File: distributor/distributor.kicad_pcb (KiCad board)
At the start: 2 copper layers, 91.5 x 52 mm, 38 parts, among them J1 Cerebellum, J10 CAN FD, J11 CAN FD, J12 CAN FD, J13 CAN FD, J14 ArmR, J15 CAN FD, J16 ArmL, J2 Cerebrum, J3 PowerBack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

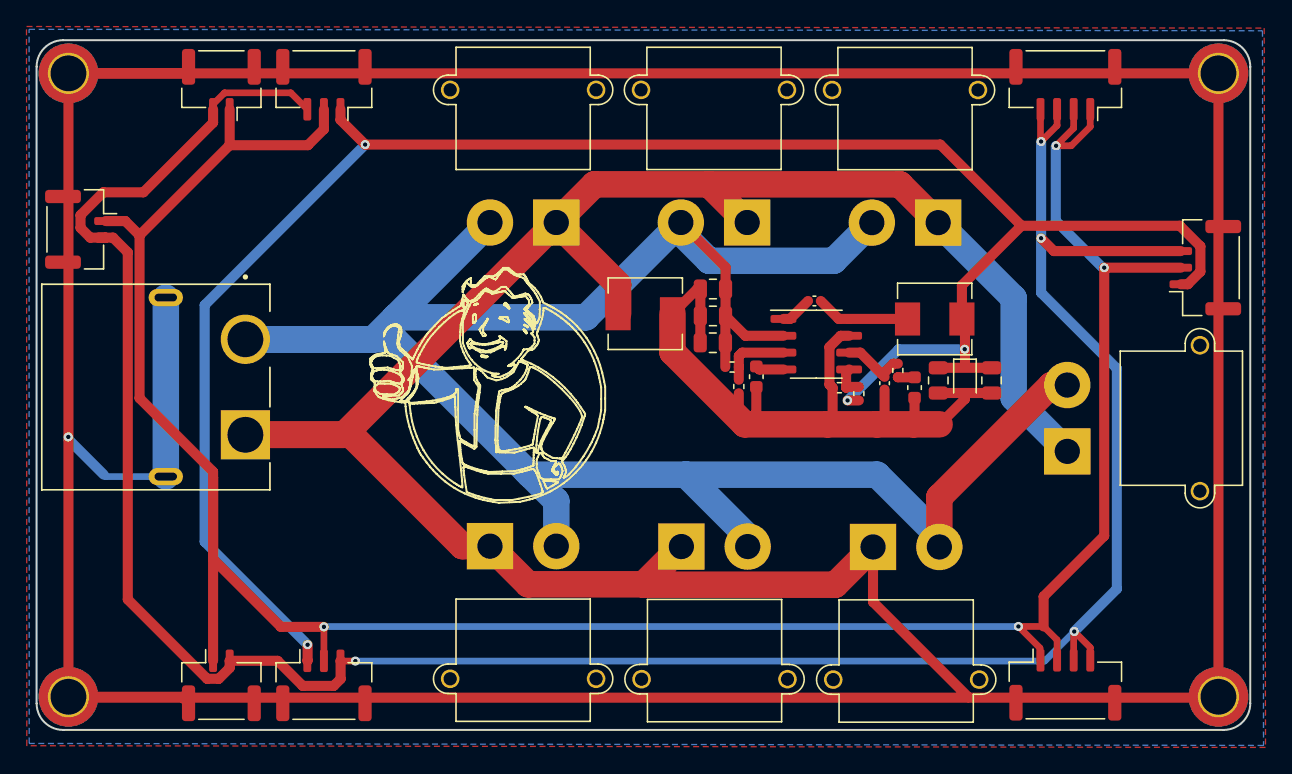
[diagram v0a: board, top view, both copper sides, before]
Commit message: [Fix] Manufacture modification
Signed-off-by: Homalozoa <nx.tardis@gmail.com>
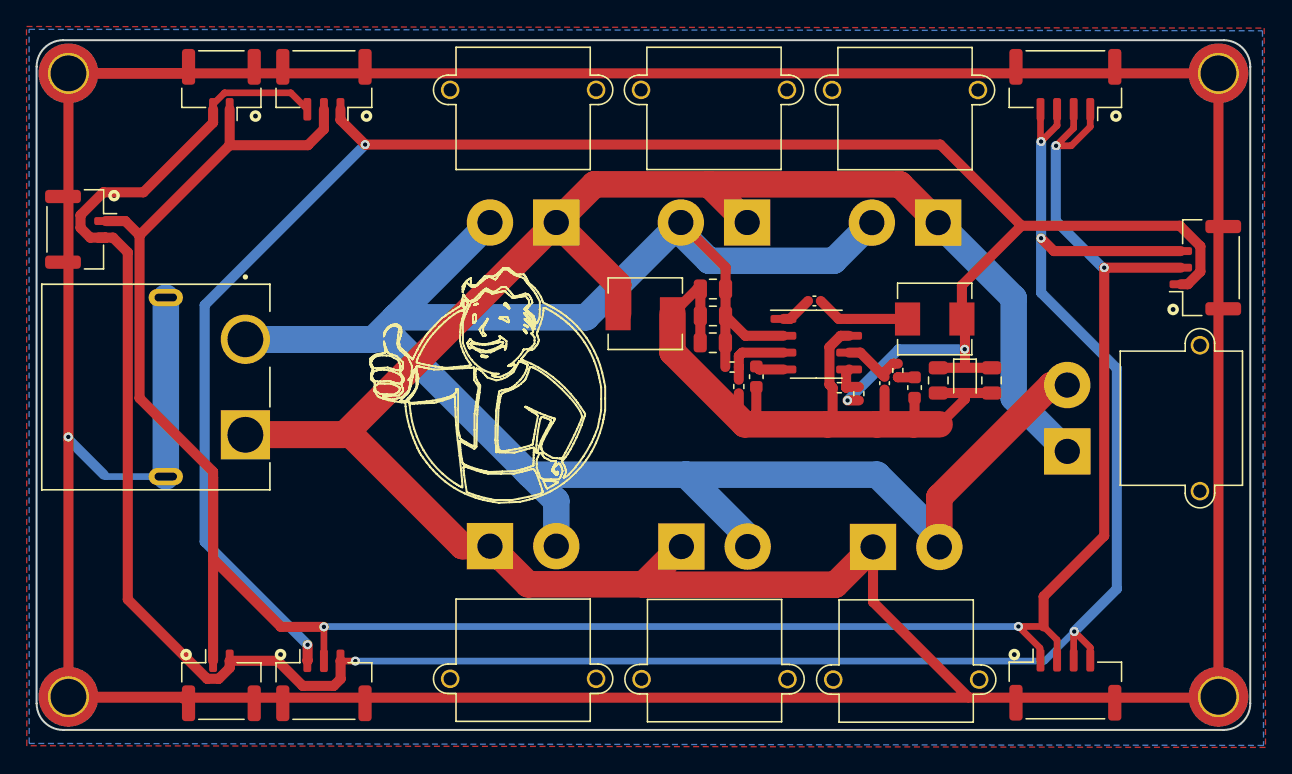
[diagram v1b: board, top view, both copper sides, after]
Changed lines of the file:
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@@
   (gr_arc (start 137.393529 98.762622) (mid 137.397287 98.760088) (end 137.401781 98.75955) (layer "F.SilkS") (width 0.15))
   (gr_line (start 143.124717 106.484575) (end 143.280318 106.639646) (layer "F.SilkS") (width 0.15))
+  (gr_circle (center 122.641 120.32) (end 122.95 120.32) (layer "F.SilkS") (width 0.254) (fill none))
   (gr_line (start 142.924024 102.971644) (end 142.689915 103.401539) (layer "F.SilkS") (width 0.15))
   (gr_arc (start 137.317254 94.651959) (mid 137.332678 94.665701) (end 137.345481 94.681916) (layer "F.SilkS") (width 0.15))
@@
   (gr_line (start 142.783427 99.367457) (end 143.299443 99.795497) (layer "F.SilkS") (width 0.15))
   (gr_line (start 131.874717 98.518776) (end 131.874717 98.292853) (layer "F.SilkS") (width 0.15))
+  (gr_circle (center 115.521 120.32) (end 115.83 120.32) (layer "F.SilkS") (width 0.254) (fill none))
   (gr_line (start 129.606263 98.677151) (end 129.57722 98.608727) (layer "F.SilkS") (width 0.15))
   (gr_line (start 138.892062 91.999983) (end 138.933694 91.937269) (layer "F.SilkS") (width 0.15))
@@
   (gr_arc (start 137.260439 95.292505) (mid 137.232883 95.299262) (end 137.204602 95.301539) (layer "F.SilkS") (width 0.15))
   (gr_line (start 146.814717 101.042419) (end 146.814717 101.917343) (layer "F.SilkS") (width 0.15))
+  (gr_circle (center 120.75 79.72) (end 121.059 79.72) (layer "F.SilkS") (width 0.254) (fill none))
   (gr_line (start 139.292217 92.954137) (end 139.419449 92.929148) (layer "F.SilkS") (width 0.15))
   (gr_line (start 139.504631 93.906628) (end 139.496372 93.92537) (layer "F.SilkS") (width 0.15))
@@
   (gr_line (start 139.404084 104.987389) (end 139.246351 104.948635) (layer "F.SilkS") (width 0.15))
   (gr_line (start 136.554061 93.608256) (end 136.579771 93.625417) (layer "F.SilkS") (width 0.15))
+  (gr_circle (center 185.621 79.72) (end 185.93 79.72) (layer "F.SilkS") (width 0.254) (fill none))
   (gr_line (start 141.105102 101.664899) (end 141.368412 101.852221) (layer "F.SilkS") (width 0.15))
   (gr_arc (start 141.504932 93.420297) (mid 141.532437 93.477727) (end 141.556662 93.536616) (layer "F.SilkS") (width 0.15))
@@
   (gr_line (start 136.395148 92.916539) (end 136.412264 92.867628) (layer "F.SilkS") (width 0.15))
   (gr_line (start 131.768438 99.378561) (end 131.775627 99.4063) (layer "F.SilkS") (width 0.15))
+  (gr_circle (center 177.961 120.32) (end 178.27 120.32) (layer "F.SilkS") (width 0.254) (fill none))
   (gr_arc (start 137.689808 100.044499) (mid 137.693473 100.054731) (end 137.694717 100.065528) (layer "F.SilkS") (width 0.15))
   (gr_line (start 139.637281 93.833144) (end 139.611227 93.821038) (layer "F.SilkS") (width 0.15))
@@
   (gr_arc (start 132.882817 98.667018) (mid 132.885181 98.633881) (end 132.894526 98.602) (layer "F.SilkS") (width 0.15))
   (gr_line (start 139.284717 91.33013) (end 139.145629 91.471269) (layer "F.SilkS") (width 0.15))
+  (gr_circle (center 189.931 94.3) (end 190.24 94.3) (layer "F.SilkS") (width 0.254) (fill none))
   (gr_line (start 135.634981 100.899169) (end 135.767217 100.841771) (layer "F.SilkS") (width 0.15))
   (gr_line (start 141.624332 96.201325) (end 141.670183 96.253625) (layer "F.SilkS") (width 0.15))
@@
   (gr_line (start 129.738205 99.987976) (end 129.723269 100.128245) (layer "F.SilkS") (width 0.15))
   (gr_arc (start 130.646649 95.864363) (mid 130.685914 95.817316) (end 130.727834 95.772618) (layer "F.SilkS") (width 0.15))
+  (gr_circle (center 110.091 85.72) (end 110.4 85.72) (layer "F.SilkS") (width 0.254) (fill none))
   (gr_arc (start 143.985993 106.972469) (mid 143.984338 106.96279) (end 143.985962 106.953108) (layer "F.SilkS") (width 0.15))
   (gr_arc (start 138.144651 97.908882) (mid 138.124538 97.910634) (end 138.104349 97.910776) (layer "F.SilkS") (width 0.15))
@@
   (gr_line (start 143.154717 107.577453) (end 142.757217 107.808681) (layer "F.SilkS") (width 0.15))
   (gr_line (start 139.670507 96.912983) (end 139.678219 96.686927) (layer "F.SilkS") (width 0.15))
+  (gr_circle (center 129.121 79.72) (end 129.43 79.72) (layer "F.SilkS") (width 0.254) (fill none))
   (gr_line (start 139.847897 95.152788) (end 139.81828 95.046692) (layer "F.SilkS") (width 0.15))
   (gr_arc (start 137.22911 93.970452) (mid 137.222514 93.962577) (end 137.225185 93.952617) (layer "F.SilkS") (width 0.15))
